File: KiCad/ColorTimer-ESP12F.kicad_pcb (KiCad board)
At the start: 2 copper layers, 1 part, among them U1 ESP-12F

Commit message: 回路図、パターン暫定版
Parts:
- added C1: 100u, Capacitor_THT:CP_Radial_D5.0mm_P2.50mm, F.Cu at (110.8, 73.0)
- added C2: 0.1u, Capacitor_THT:C_Disc_D3.0mm_W1.6mm_P2.50mm, F.Cu at (109.8, 69.8)
- added C3: 0.1u, Capacitor_THT:C_Disc_D3.0mm_W1.6mm_P2.50mm, F.Cu at (123.5, 67.8)
- added C4: 10u, Capacitor_THT:CP_Radial_D5.0mm_P2.50mm, F.Cu at (120.2, 65.2)
- added D1: RED LED, LED_THT:LED_D3.0mm, F.Cu at (128.3, 82.2)
- added D2: BLUE LED, LED_THT:LED_D3.0mm, F.Cu at (137.6, 82.0)
- added H1: MountingHole, MountingHole:MountingHole_3.2mm_M3, F.Cu at (99.0, 44.0)
- added H2: MountingHole, MountingHole:MountingHole_3.2mm_M3, F.Cu at (100.5, 85.5)
- added H3: MountingHole, MountingHole:MountingHole_3.2mm_M3, F.Cu at (165.5, 44.0)
- added H4: MountingHole, MountingHole:MountingHole_3.2mm_M3, F.Cu at (165.5, 86.0)
- added J1: SERIAL CON, Connector_PinHeader_2.54mm:PinHeader_1x06_P2.54mm_Horizontal, F.Cu at (162.8, 51.1)
- added J2: GPIO_CON, Connector_PinSocket_2.54mm:PinSocket_1x09_P2.54mm_Vertical, F.Cu at (157.5, 43.9)
- added J3: Barrel_Jack_Switch, Connector_BarrelJack:BarrelJack_Horizontal, F.Cu at (104.5, 72.5)
- added J4: RED_CON, Connector_PinSocket_2.54mm:PinSocket_1x02_P2.54mm_Vertical, F.Cu at (120.8, 85.2)
- added J5: BLUE_CON, Connector_PinSocket_2.54mm:PinSocket_1x02_P2.54mm_Vertical, F.Cu at (111.2, 85.2)
- added J6: SW_CON, Connector_PinSocket_2.54mm:PinSocket_1x02_P2.54mm_Vertical, F.Cu at (165.2, 78.5)
- added JP1: Power JP, Connector_PinHeader_2.54mm:PinHeader_1x02_P2.54mm_Vertical, F.Cu at (163.2, 69.0)
- added R1: 10k, Resistor_THT:R_Axial_DIN0207_L6.3mm_D2.5mm_P10.16mm_Horizontal, F.Cu at (118.8, 58.8)
- added R2: 10k, Resistor_THT:R_Axial_DIN0207_L6.3mm_D2.5mm_P10.16mm_Horizontal, F.Cu at (115.5, 58.8)
- added R3: 10k, Resistor_THT:R_Axial_DIN0207_L6.3mm_D2.5mm_P10.16mm_Horizontal, F.Cu at (145.1, 60.6)
- added R4: 10k, Resistor_THT:R_Axial_DIN0207_L6.3mm_D2.5mm_P10.16mm_Horizontal, F.Cu at (148.8, 57.8)
- added R5: 10k, Resistor_THT:R_Axial_DIN0207_L6.3mm_D2.5mm_P10.16mm_Horizontal, F.Cu at (145.1, 57.7)
- added R6: 10k, Resistor_THT:R_Axial_DIN0207_L6.3mm_D2.5mm_P10.16mm_Horizontal, F.Cu at (158.7, 73.6)
- added R7: 330, Resistor_THT:R_Axial_DIN0207_L6.3mm_D2.5mm_P10.16mm_Horizontal, F.Cu at (139.2, 71.2)
- added R8: 330, Resistor_THT:R_Axial_DIN0207_L6.3mm_D2.5mm_P10.16mm_Horizontal, F.Cu at (139.2, 75.0)
- added SW1: RESET, Button_Switch_THT:SW_PUSH_6mm_H8mm, F.Cu at (111.0, 49.5)
- added SW2: FLASH, Button_Switch_THT:SW_PUSH_6mm_H8mm, F.Cu at (111.0, 58.5)
- added SW3: Trigger SW, Button_Switch_THT:SW_PUSH_6mm_H8mm, F.Cu at (145.1, 79.8)
- added SW4: POWER_SW, Connector_PinHeader_2.54mm:PinHeader_1x03_P2.54mm_Vertical, F.Cu at (98.7, 64.0)
- added U2: L78L33_TO92, Package_TO_SOT_THT:TO-92_Inline_Wide, F.Cu at (114.6, 65.0)
- moved U1 50.2 mm to (125.0, 48.9)
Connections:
- U1 pad 1: unconnected-(U1-REST-Pad1) -> Net-(U1-REST)
- U1 pad 10: unconnected-(U1-GPIO15-Pad10) -> Net-(U1-GPIO15)
- U1 pad 11: unconnected-(U1-GPIO2-Pad11) -> Net-(U1-GPIO2)
- U1 pad 12: unconnected-(U1-GPIO0-Pad12) -> Net-(U1-GPIO0)
- U1 pad 13: unconnected-(U1-GPIO4-Pad13) -> /GPIO4
- U1 pad 14: unconnected-(U1-GPIO5-Pad14) -> /GPIO5
- U1 pad 15: unconnected-(U1-RXD-Pad15) -> Net-(J1-Pin_4)
- U1 pad 16: unconnected-(U1-TXD-Pad16) -> Net-(J1-Pin_5)
- U1 pad 2: unconnected-(U1-ADC-Pad2) -> /ADC
- U1 pad 3: unconnected-(U1-CH_PD-Pad3) -> Net-(U1-CH_PD)
- U1 pad 4: unconnected-(U1-GPIO16-Pad4) -> /GPIO16
- U1 pad 5: unconnected-(U1-GPIO14-Pad5) -> /GPIO14
- U1 pad 6: unconnected-(U1-GPIO12-Pad6) -> /GPIO12
- U1 pad 7: unconnected-(U1-GPIO13-Pad7) -> /GPIO13
- U1 pad 8: unconnected-(U1-VCC-Pad8) -> +3.3V
- U1 pad 9: unconnected-(U1-GND-Pad9) -> GND
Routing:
- net GND: track 0.00 -> 103.6 mm, vias 0 -> 1
- net +3.3V: track 0.00 -> 19.9 mm
- net Net-(SW4-B): track 0.00 -> 19.4 mm
- net Net-(SW4-A): track 0.00 -> 10.9 mm
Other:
- board outline added: 74.5 x 50 mm
- board text added: "+3.3V"
- board text added: "10k"
- board text added: "10u"
- board text added: "330"
- board text added: "78L33"
- board text added: "ADC"
- board text added: "BLUE CON"
- board text added: "BLUE LED"
- board text added: "COLOR TIMER REV1 KUNI-NET 2025"
- board text added: "ESP-12F"
- board text added: "FLASH"
- board text added: "GND"
- board text added: "IO12"
- board text added: "IO13"
- board text added: "IO14"
- board text added: "IO16"
- board text added: "IO4"
- board text added: "IO5"
- board text added: "ON OFF"
- board text added: "POWER_JP"
- board text added: "RED CON"
- board text added: "RED LED"
- board text added: "RESET"
- board text added: "SW CON"
- board text added: "TRIGGER SW"

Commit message: 部品の関連付けなど
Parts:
- removed JP1: Power JP, Connector_PinHeader_2.54mm:PinHeader_1x02_P2.54mm_Vertical
- added C5: 0.1u, Capacitor_THT:C_Disc_D3.0mm_W1.6mm_P2.50mm, F.Cu at (80.5, 63.9)
- added C6: 0.1u, Capacitor_THT:C_Disc_D3.0mm_W1.6mm_P2.50mm, F.Cu at (80.5, 67.1)
- added C7: 10u, Capacitor_THT:CP_Radial_D5.0mm_P2.50mm, F.Cu at (87.8, 51.8)
- added D3: POWER LED, LED_THT:LED_D3.0mm, F.Cu at (88.7, 59.3)
- added F1: 350mA, Fuse:Fuse_1206_3216Metric_Pad1.42x1.75mm_HandSolder, F.Cu at (87.5, 64.0)
- added Q1: 2N7000, Package_TO_SOT_THT:TO-92_Inline, F.Cu at (74.4, 59.8)
- added Q2: 2N7000, Package_TO_SOT_THT:TO-92_Inline, F.Cu at (74.4, 65.6)
- added R10: 330, Resistor_THT:R_Axial_DIN0207_L6.3mm_D2.5mm_P10.16mm_Horizontal, F.Cu at (74.0, 54.5)
- added R9: 10k, Resistor_THT:R_Axial_DIN0207_L6.3mm_D2.5mm_P10.16mm_Horizontal, F.Cu at (74.0, 50.5)
- added U3: L78L33_TO92, Package_TO_SOT_THT:TO-92_Inline_Wide, F.Cu at (80.4, 59.8)
- C1: value 100u -> 0.1u; footprint Capacitor_THT:CP_Radial_D5.0mm_P2.50mm -> Capacitor_THT:C_Disc_D3.0mm_W1.6mm_P2.50mm
- C3: value 0.1u -> 10u
- C4: value 10u -> 0.1u; footprint Capacitor_THT:CP_Radial_D5.0mm_P2.50mm -> Capacitor_THT:C_Disc_D3.0mm_W1.6mm_P2.50mm
- J1: value SERIAL CON -> SW_CON; footprint Connector_PinHeader_2.54mm:PinHeader_1x06_P2.54mm_Horizontal -> Connector_PinSocket_2.54mm:PinSocket_1x02_P2.54mm_Vertical
- J2: value GPIO_CON -> USB_B_Micro; footprint Connector_PinSocket_2.54mm:PinSocket_1x09_P2.54mm_Vertical -> Connector_USB:USB_Micro-B_Molex-105017-0001
- J3: value Barrel_Jack_Switch -> COLOER_LED; footprint Connector_BarrelJack:BarrelJack_Horizontal -> Connector_PinSocket_2.54mm:PinSocket_1x03_P2.54mm_Vertical
- J4: value RED_CON -> AkitsukiCON; footprint Connector_PinSocket_2.54mm:PinSocket_1x02_P2.54mm_Vertical -> Connector_PinSocket_2.54mm:PinSocket_1x05_P2.54mm_Vertical
- J5: value BLUE_CON -> GPIO_CON; footprint Connector_PinSocket_2.54mm:PinSocket_1x02_P2.54mm_Vertical -> Connector_PinSocket_2.54mm:PinSocket_1x09_P2.54mm_Vertical
- J6: value SW_CON -> POWER_CON
- R4, R5: value 10k -> 330
- R6: value 10k -> 33
- R7, R8: value 330 -> 10k
- SW2: value FLASH -> Trigger SW
- SW3: value Trigger SW -> FLASH
- SW4: value POWER_SW -> SW_SPDT; footprint Connector_PinHeader_2.54mm:PinHeader_1x03_P2.54mm_Vertical -> Connector_PinSocket_2.54mm:PinSocket_1x03_P2.54mm_Vertical
- U2: value L78L33_TO92 -> CH340K; footprint Package_TO_SOT_THT:TO-92_Inline_Wide -> Package_SO:SSOP-10-1EP_3.9x4.9mm_P1mm_EP2.1x3.3mm
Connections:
- C1 pad 1: Net-(SW4-B) -> Net-(U1-REST)
- C2 pad 1: Net-(SW4-B) -> +3.3V
- C3 pad 1: +3.3V -> VCC
- J1 pad 1: GND -> /GPIO16
- J1 pad 2: Net-(J1-Pin_2) -> GND
- J2 pad 1: /GPIO4 -> Net-(J2-VBUS)
- J2 pad 2: /GPIO5 -> Net-(J2-D-)
- J2 pad 3: /GPIO12 -> Net-(J2-D+)
- J2 pad 4: /GPIO13 -> unconnected-(J2-ID-Pad4)
- J2 pad 5: /GPIO14 -> GND
- J2 pad 6: /GPIO16 -> GND
- J3 pad 1: Net-(SW4-A) -> /GPIO13
- J3 pad 2: GND -> Net-(J3-Pin_2)
- J3 pad 3: GND -> /GPIO12
- J4 pad 1: Net-(D1-A) -> VCC
- J4 pad 2: GND -> Net-(J2-D+)
- J5 pad 1: Net-(D2-A) -> /GPIO4
- J5 pad 2: GND -> /GPIO5
- J6 pad 1: /GPIO16 -> +5V
- J6 pad 2: GND -> VCC
- R2 pad 2: Net-(U1-CH_PD) -> /GPIO16
- R3 pad 1: Net-(U1-GPIO15) -> +3.3V
- R3 pad 2: GND -> EN
- R4 pad 1: +3.3V -> Net-(D1-A)
- R4 pad 2: Net-(U1-GPIO2) -> /GPIO13
- R5 pad 1: +3.3V -> Net-(D2-A)
- R5 pad 2: Net-(U1-GPIO0) -> /GPIO12
- R6 pad 1: +3.3V -> GND
- R6 pad 2: /GPIO16 -> Net-(J3-Pin_2)
- R7 pad 1: Net-(D1-A) -> +3.3V
- R7 pad 2: /GPIO14 -> GPIO0
- R8 pad 1: Net-(D2-A) -> Net-(U1-GPIO15)
- R8 pad 2: /GPIO13 -> GND
- SW2 pad 1: Net-(U1-GPIO0) -> GND
- SW2 pad 2: GND -> /GPIO16
- SW3 pad 1: GND -> GPIO0
- SW3 pad 2: /GPIO16 -> GND
- SW4 pad 1: Net-(SW4-A) -> VCC
- SW4 pad 2: Net-(SW4-B) -> +5V
- SW4 pad 3: (no net) -> unconnected-(SW4-C-Pad3)
- U1 pad 12: Net-(U1-GPIO0) -> GPIO0
- U1 pad 15: Net-(J1-Pin_4) -> RxD
- U1 pad 16: Net-(J1-Pin_5) -> TxD
- U1 pad 3: Net-(U1-CH_PD) -> EN
- U2 pad 1: +3.3V -> Net-(J2-D+)
- U2 pad 2: GND -> Net-(J2-D-)
- U2 pad 3: Net-(SW4-B) -> GND
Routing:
- net GND: track 103.6 -> 0.00 mm, vias 1 -> 0
- net +3.3V: track 19.9 -> 0.00 mm
- net Net-(SW4-B): track 19.4 -> 0.00 mm
- net Net-(SW4-A): track 10.9 -> 0.00 mm

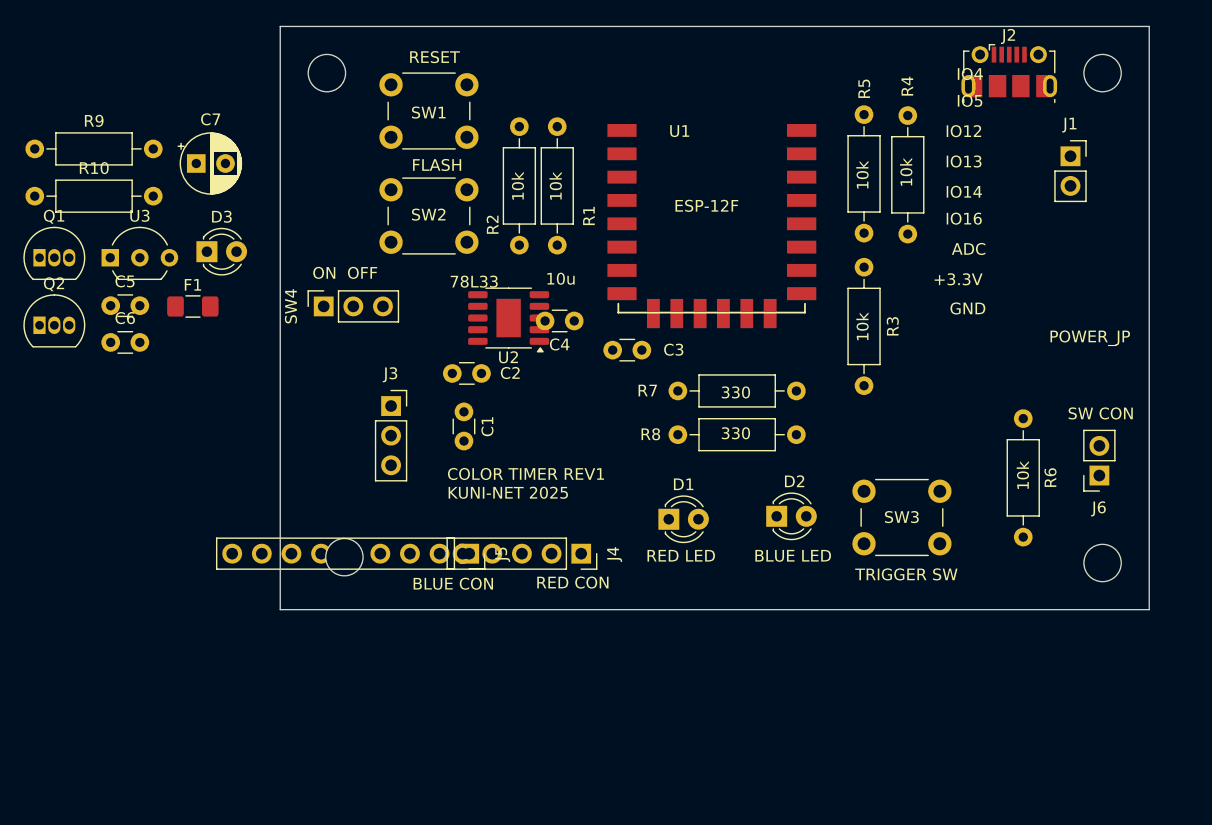
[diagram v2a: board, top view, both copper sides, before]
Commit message: コンデンサ等調整、AE-USB^MICRO-Bフットプリント追加
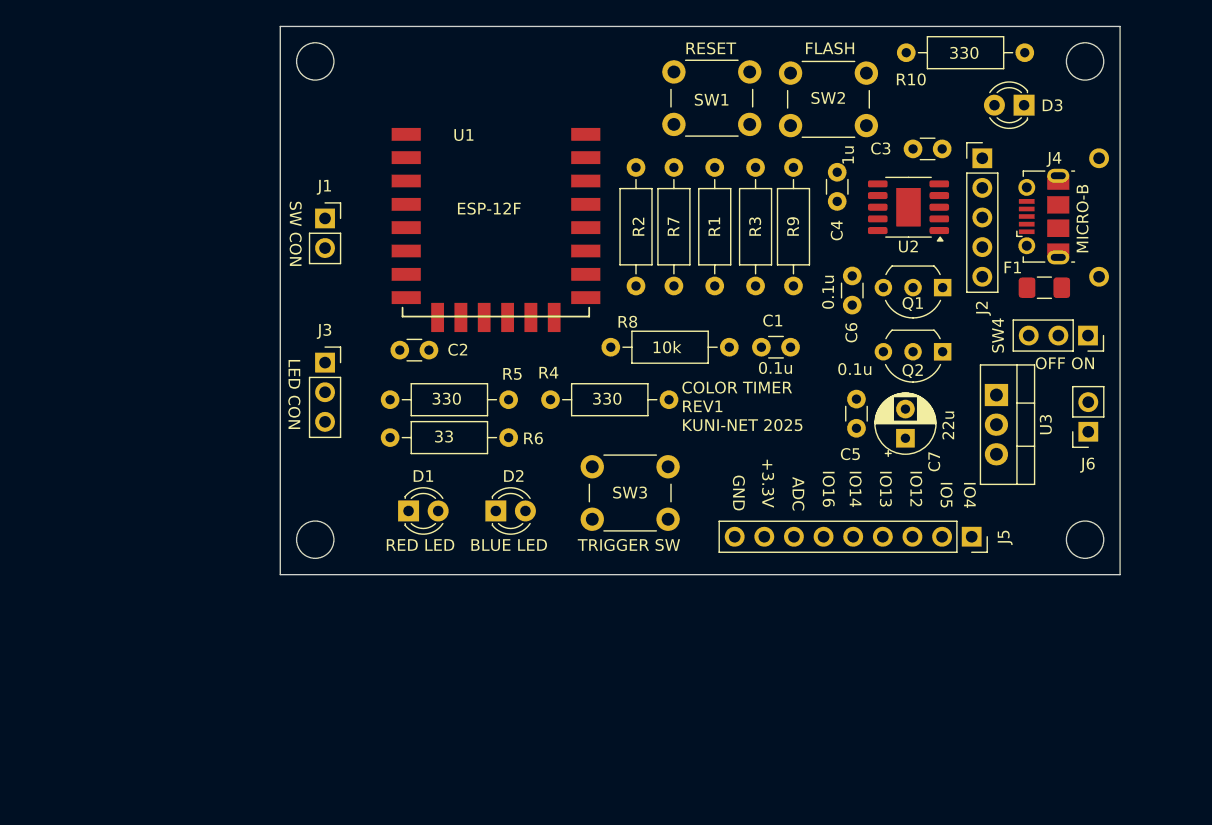
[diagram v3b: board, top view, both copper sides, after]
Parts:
- C4: value 0.1u -> 1u
- C7: value 10u -> 22u
- J4: footprint Connector_PinSocket_2.54mm:PinSocket_1x05_P2.54mm_Vertical -> AE:AE-USB-MICRO-B-D
- Q1, Q2: footprint Package_TO_SOT_THT:TO-92_Inline -> Package_TO_SOT_THT:TO-92_Inline_Wide
- U3: value L78L33_TO92 -> BA033CC0T_TO220; footprint Package_TO_SOT_THT:TO-92_Inline_Wide -> Package_TO_SOT_THT:TO-220-3_Vertical
- moved Q1 77.5 mm to (151.8, 62.4), turned to 180 degrees
- moved Q2 77.5 mm to (151.8, 67.9), turned to 180 degrees
- moved U3 76.9 mm to (156.4, 71.6), turned to -90 degrees
- moved R10 75.7 mm to (148.7, 42.2)
- moved F1 73.0 mm to (160.5, 62.4)
- moved D3 71.2 mm to (158.8, 46.8), turned to 180 degrees
- moved SW4 65.6 mm to (164.2, 66.5), turned to -90 degrees
- moved C7 65.2 mm to (148.6, 75.3), turned to 90 degrees
- moved R9 65.1 mm to (139.0, 52.1), turned to -90 degrees
- moved C5 64.4 mm to (144.4, 72.0), turned to -90 degrees
- moved J1 64.1 mm to (98.8, 56.5)
- moved C6 63.8 mm to (144.0, 61.4), turned to -90 degrees
- moved J4 49.3 mm to (160.3, 55.7), turned to 0 degrees
- moved R6 44.2 mm to (114.6, 75.2), turned to 180 degrees
- moved J5 43.1 mm to (154.3, 83.8)
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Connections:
- U3 pad 1: +3.3V -> +5V
- U3 pad 3: +5V -> +3.3V
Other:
- board size 74.5 x 50 mm -> 72 x 47 mm
- board text added: "0.1u"
- board text added: "1u"
- board text added: "22u"
- board text added: "33"
- board text added: "LED CON"
- board text added: "MICRO-B"
- board text added: "OFF ON"
- board text removed: "10u"
- board text removed: "78L33"
- board text removed: "BLUE CON"
- board text removed: "ON OFF"
- board text removed: "POWER_JP"
- board text removed: "RED CON"

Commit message: 回路間違い修正 & ガーバー出力
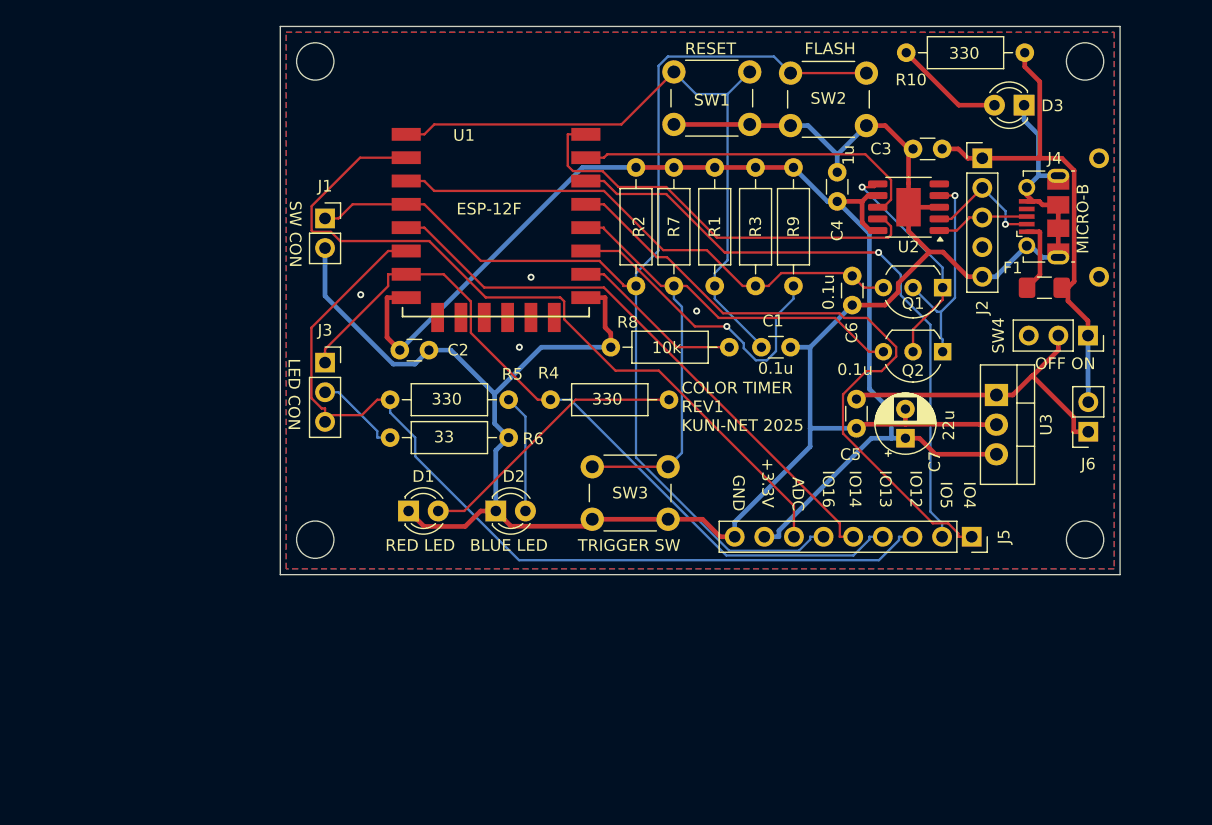
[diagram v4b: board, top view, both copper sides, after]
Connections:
- J4 pad 2: Net-(J2-D+) -> Net-(J2-D-)
- J4 pad 3: Net-(J2-D-) -> Net-(J2-D+)
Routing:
- net GND: track 0.00 -> 205.0 mm, vias 0 -> 4
- net +3.3V: track 0.00 -> 106.1 mm
- net /GPIO16: track 0.00 -> 103.3 mm
- net /GPIO12: track 0.00 -> 79.5 mm
- net /ADC: track 0.00 -> 67.3 mm
- net /GPIO13: track 0.00 -> 64.6 mm
- net /GPIO4: track 0.00 -> 57.3 mm
- net Net-(U1-REST): track 0.00 -> 56.4 mm
- net /GPIO5: track 0.00 -> 55.0 mm, vias 0 -> 1
- net GPIO0: track 0.00 -> 53.5 mm
- net /GPIO14: track 0.00 -> 49.3 mm
- net EN: track 0.00 -> 44.9 mm
- net VCC: track 0.00 -> 43.0 mm
- net TxD: track 0.00 -> 36.0 mm
- net RxD: track 0.00 -> 31.0 mm
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- added copper zone on B.Cu, net GND
- added copper zone on F.Cu, net GND

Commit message: 微修正、ガーバー再出力
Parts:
- R10: value 330 -> 1k
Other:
- board text added: "1k"
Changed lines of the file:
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@@
 			)
 		)
-		(property "Value" "330"
+		(property "Value" "1k"
 			(at 5.08 1.37 0)
 			(layer "F.Fab")
@@
 		)
 	)
-	(gr_text "330"
+	(gr_text "1k"
 		(at 152.33 42.89 0)
 		(layer "F.SilkS")
